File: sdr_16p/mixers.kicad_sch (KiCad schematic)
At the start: 48 parts, among them U11 74CBT1G125DBVRE4, U12 74CBT1G125DBVRE4, U13 74CBT1G125DBVRE4, U14 74CBT1G125DBVRE4, U16 74CBT1G125DBVRE4, U17 74CBT1G125DBVRE4, U18 74CBT1G125DBVRE4, U19 74CBT1G125DBVRE4, U22 74CBT1G125DBVRE4, U24 74CBT1G125DBVRE4, U26 74CBT1G125DBVRE4, U28 74CBT1G125DBVRE4, U30 74CBT1G125DBVRE4, U32 74CBT1G125DBVRE4, U34 74CBT1G125DBVRE4, U6 74CBT1G125DBVRE4

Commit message: added holding cap and dc blocking cap
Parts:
- added C1, C106, C107, C108, C109, C110, C111, C112, C113, C114, C115, C116, C117, C119, C120, C121: 130p, Capacitor_SMD:C_0402_1005Metric_Pad0.74x0.62mm_HandSolder, symbol Device:C_Small
- added C100, C101, C102, C103, C104, C105, C2, C87, C88, C90, C91, C94, C95, C96, C97, C99: 0.1u, Capacitor_SMD:C_0603_1608Metric_Pad1.08x0.95mm_HandSolder, symbol Device:C_Small
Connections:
- net GND: now also C1.2, C106.2, C107.2, C108.2, C109.2, C110.2, C111.2, C112.2, C113.2, C114.2, C115.2, C116.2, C117.2, C119.2, C120.2, C121.2
- net NZIF0: now also C2.2; no longer U6.4 (B)
- net NZIF1: now also C87.2; no longer U17.4 (B)
- net NZIF10: now also C100.2; no longer U32.4 (B)
- net NZIF11: now also C101.2; no longer U34.4 (B)
- net NZIF12: now also C102.2; no longer U11.4 (B)
- net NZIF13: now also C103.2; no longer U14.4 (B)
- net NZIF14: now also C104.2; no longer U18.4 (B)
- net NZIF15: now also C105.2; no longer U16.4 (B)
- net NZIF2: now also C88.2; no longer U24.4 (B)
- net NZIF3: now also C90.2; no longer U26.4 (B)
- net NZIF4: now also C91.2; no longer U12.4 (B)
- net NZIF5: now also C94.2; no longer U19.4 (B)
- net NZIF6: now also C95.2; no longer U28.4 (B)
- net NZIF7: now also C96.2; no longer U30.4 (B)
- net NZIF8: now also C97.2; no longer U13.4 (B)
- net NZIF9: now also C99.2; no longer U22.4 (B)
- new net: C105.1, C121.1, U16.4 (B)
- new net: C106.1, C87.1, U17.4 (B)
- new net: C108.1, C90.1, U26.4 (B)
- new net: C103.1, C119.1, U14.4 (B)
- new net: C101.1, C116.1, U34.4 (B)
- new net: C111.1, C95.1, U28.4 (B)
- new net: C114.1, C99.1, U22.4 (B)
- new net: C104.1, C120.1, U18.4 (B)
- new net: C1.1, C2.1, U6.4 (B)
- new net: C107.1, C88.1, U24.4 (B)
- new net: C112.1, C96.1, U30.4 (B)
- new net: C100.1, C115.1, U32.4 (B)
- new net: C110.1, C94.1, U19.4 (B)
- new net: C113.1, C97.1, U13.4 (B)
- new net: C102.1, C117.1, U11.4 (B)
- new net: C109.1, C91.1, U12.4 (B)
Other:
- note added: "0402 0.1u caps need to be placed right at VCC in with no trace to ground (use via) Holding cap is also 0402 to minimize inductance. Blocking cap is at baseband, so we can switch to 0603 for easier soldering and rework"
- note added: "Antenna R = 50 Transformed R = 16 * 50 = 800(transformer is 1:4) Effective R = N * 800 = 800 ohm (N = 16 phases) Desired BW = 96khz (Nyquist with 192khz sampling rate) BW = 1 / (2*pi*R*C) => C = 130pF"
- note added: "The 0.1uF output cap blocks DC, creating a isolation of the mixer along with the transformer. This will allow ADAU1978 to set the bias with the fully differential driver amp. It also provides a hpf with cutoff of 1 / (2*pi*(12800 + 10000)*0.1u) = 70Hz 10000 comes from the R of the FDA. 12800 comes from 16 * 800"
- note removed: "0402 0.1u caps need to be placed right at VCC in with no trace to ground (use via)"
- moved on the sheet: C10, C11, C12, C13, C14, C15, C16, C17, C18, C19, C20, C21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

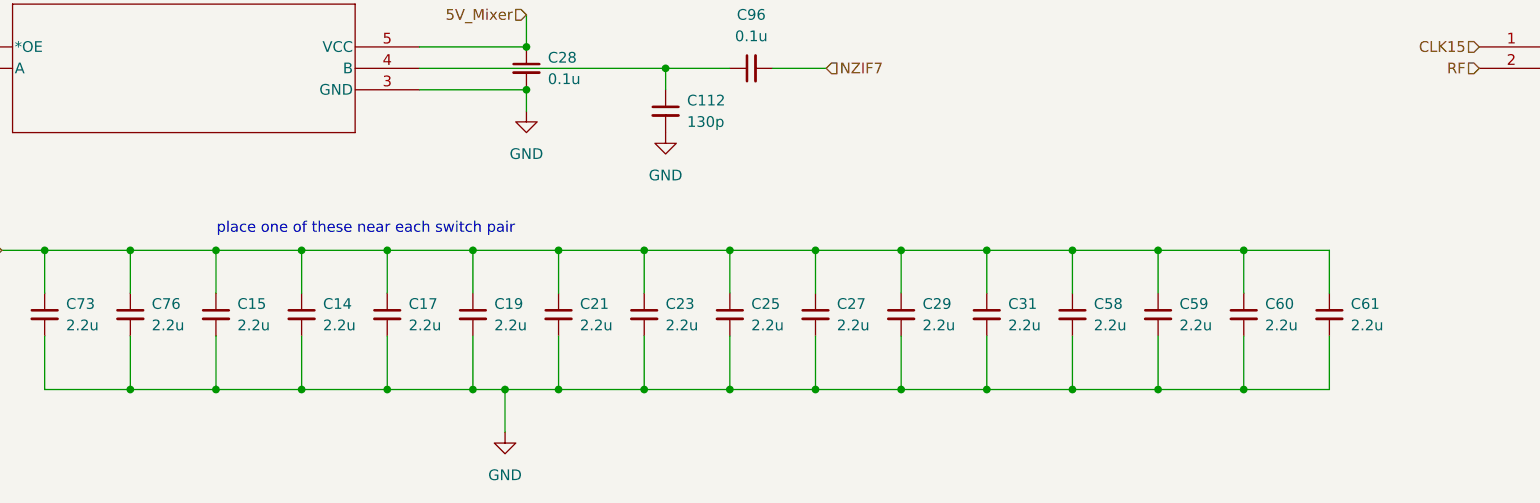
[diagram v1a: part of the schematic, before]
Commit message: updated cap sizes
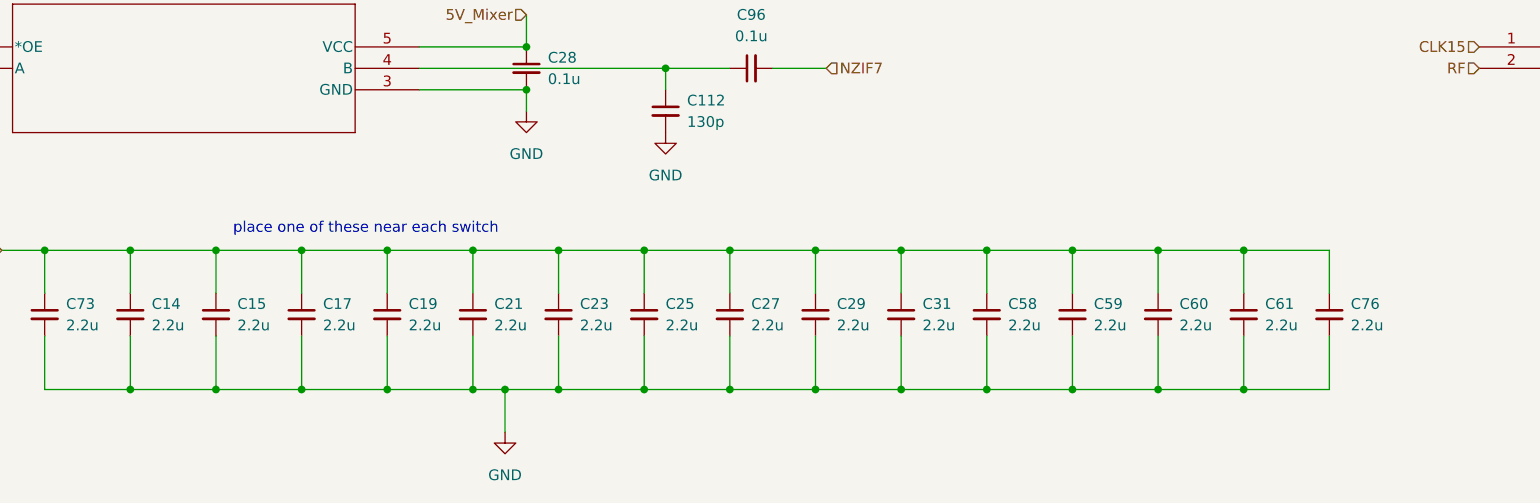
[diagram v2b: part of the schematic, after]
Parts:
- C14, C15, C17, C19, C21, C23, C25, C27, C29, C31, C58, C59, C60, C61, C73, C76: footprint (none) -> Capacitor_SMD:C_0603_1608Metric_Pad1.08x0.95mm_HandSolder
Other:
- note added: "place one of these near each switch"
- note removed: "place one of these near each switch pair"

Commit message: updated crosspoint
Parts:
- renumbered C121 to C?, C28 to C?, C21 to C?, C87 to C?, C76 to C?, C119 to C?, C95 to C?, C9 to C?, C114 to C?, C22 to C?, C23 to C?, C104 to C?, C29 to C?, C107 to C?, C20 to C?, C6 to C?, C8 to C?, C100 to C?, C94 to C?, C110 to C?, C16 to C?, C73 to C?, C10 to C?, C115 to C?, C59 to C?, C24 to C?, C13 to C?, C106 to C?, C58 to C?, C116 to C?, C103 to C?, C102 to C?, C96 to C?, C88 to C?, C27 to C?, C105 to C?, C18 to C?, C113 to C?, C25 to C?, C90 to C?, C108 to C?, C60 to C?, C117 to C?, C91 to C?, C61 to C?, C31 to C?, C111 to C?, C19 to C?, C120 to C?, C17 to C?, C15 to C?, C99 to C?, C112 to C?, C101 to C?, C26 to C?, C109 to C?, C30 to C?, C97 to C?, C32 to C?, C11 to C?, C12 to C?, C14 to C?, U26 to U?, U34 to U?, U30 to U?, U17 to U?, U18 to U?, U13 to U?, U12 to U?, U28 to U?, U14 to U?, U19 to U?, U6 to U?, U22 to U?, U24 to U?, U16 to U?, U11 to U?, U32 to U?
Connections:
- net NZIF0 renamed Phase_0
- net NZIF1 renamed Phase_1
- net NZIF10 renamed Phase_10
- net NZIF11 renamed Phase_11
- net NZIF12 renamed Phase_12
- net NZIF13 renamed Phase_13
- net NZIF14 renamed Phase_14
- net NZIF15 renamed Phase_15
- net NZIF2 renamed Phase_2
- net NZIF3 renamed Phase_3
- net NZIF4 renamed Phase_4
- net NZIF5 renamed Phase_5
- net NZIF6 renamed Phase_6
- net NZIF7 renamed Phase_7
- net NZIF8 renamed Phase_8
- net NZIF9 renamed Phase_9
